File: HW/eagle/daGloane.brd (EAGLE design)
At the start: 182.4 x 160.7 mm, 65 parts, among them IC1 MCP1252-33X50, U1 STM32F10XTXU6, X2 SPARKFUN-CONNECTORS_USB-MICROB

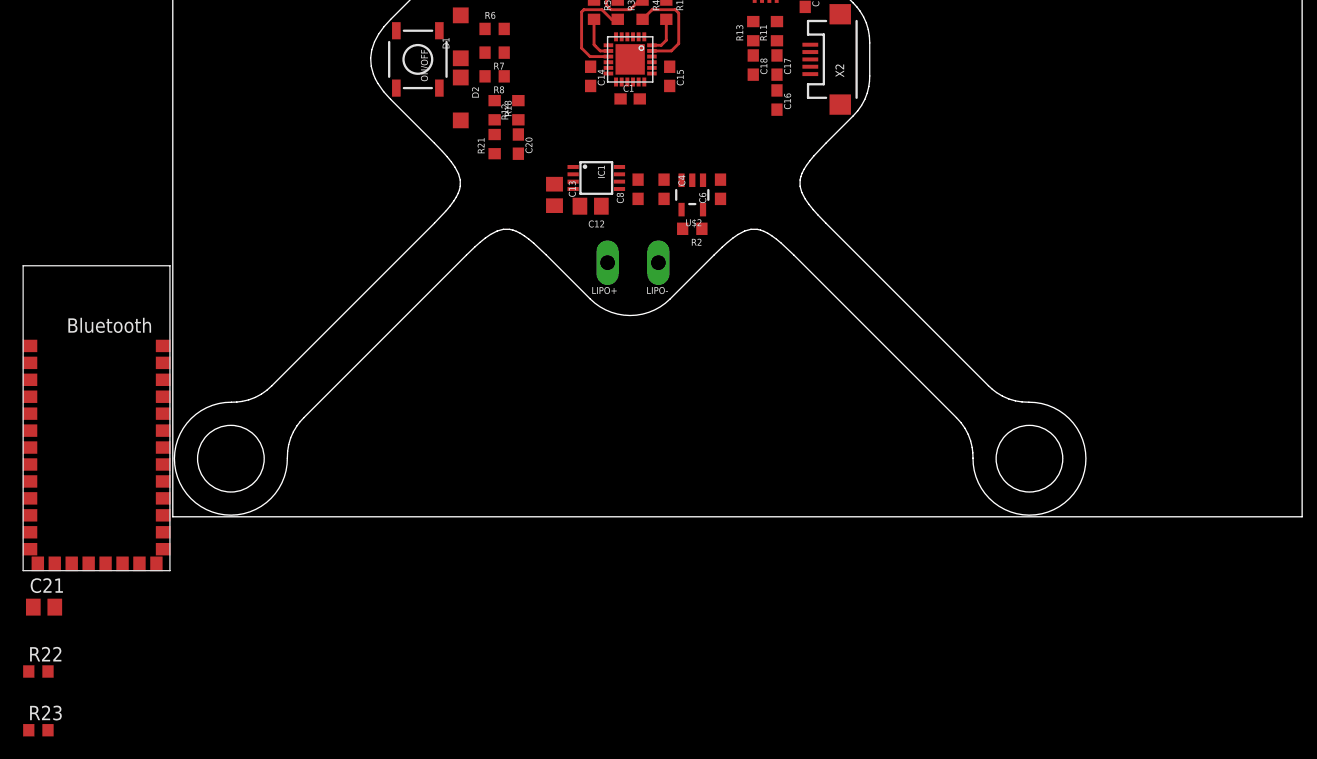
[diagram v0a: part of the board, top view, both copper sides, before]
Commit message: missing connection uart connection to bluetooth module fixed
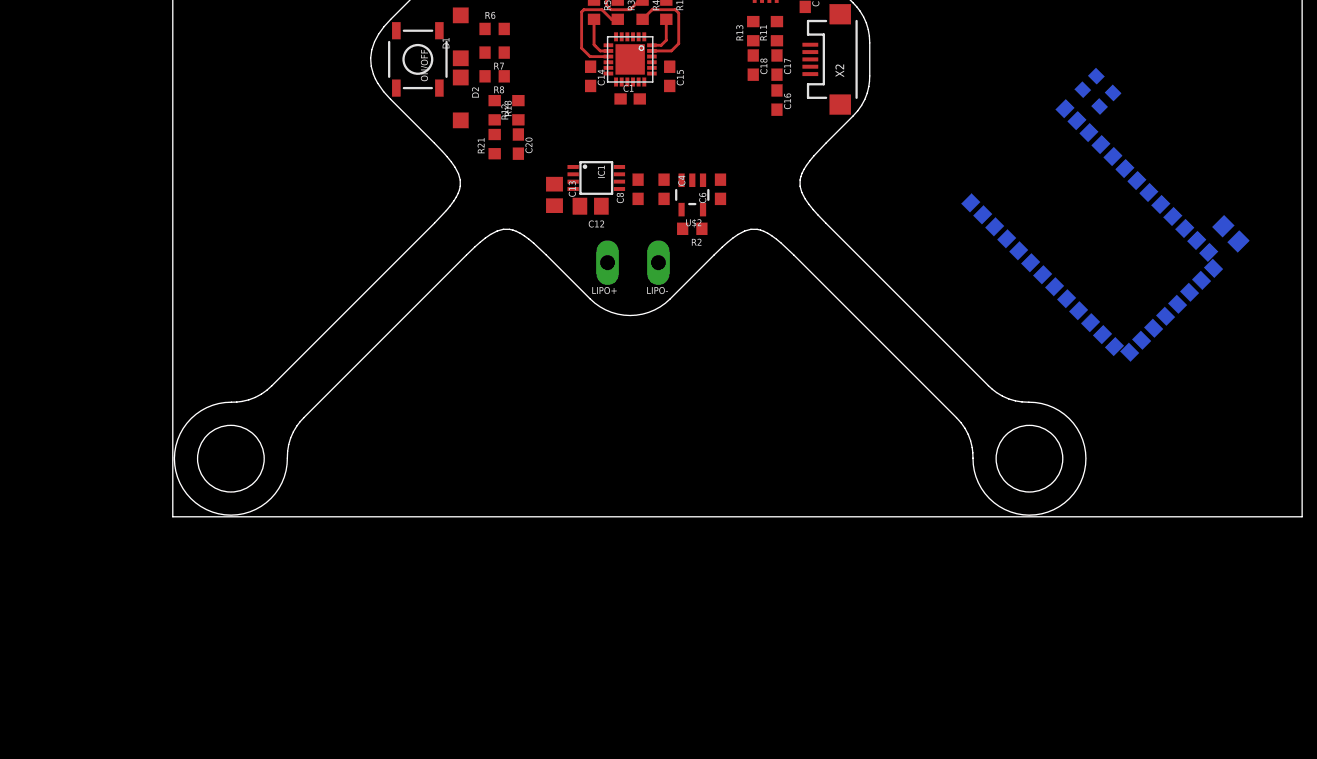
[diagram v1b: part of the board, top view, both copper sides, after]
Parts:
- moved C21 110.2 mm to (93.7, 25.1), flipped to the bottom, turned to 225 degrees
- moved R23 109.8 mm to (82.7, 36.9), flipped to the bottom, turned to 315 degrees
- moved R22 106.7 mm to (81.2, 38.4), flipped to the bottom, turned to 315 degrees
- moved U$5 86.8 mm to (78.0, 29.0), flipped to the bottom, turned to 315 degrees
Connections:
- net USART2_RX: now also R22.1
- net USART2_TX: now also R23.1
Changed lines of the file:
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@@
 <?xml version="1.0" encoding="utf-8"?>
 <!DOCTYPE eagle SYSTEM "eagle.dtd">
-<eagle version="6.2">
+<eagle version="6.1">
 <drawing>
 <settings>
@@
 <board>
 <plain>
-<wire x1="-0.000003125" y1="-4.9999875" x2="0.00000625" y2="-4.999996875" width="0.01" layer="20"/>
 <wire x1="84.99998125" y1="-0.000003125" x2="84.999990625" y2="0.00000625" width="0.01" layer="20"/>
-<wire x1="78.5" y1="84.49998125" x2="78.499990625" y2="84.499990625" width="0.01" layer="20"/>
 <wire x1="0" y1="0" x2="0" y2="80" width="0.01" layer="20"/>
 <wire x1="0" y1="80" x2="100" y2="80" width="0.01" layer="20"/>
@@
 </element>
 <element name="X2" library="daGloane" package="SPARKFUN-CONNECTORS_USB-MICROB" value="SPARKFUN-CONNECTORS_USB-MICROB" x="59.1" y="40.5" rot="R90"/>
-<element name="U$5" library="daGloane" package="BLUETOOTH" value="BLUETOOTH" x="-6.9" y="10.8"/>
-<element name="C21" library="rcl" package="C0805" value="10µF/6.3V" x="-11.4" y="-8"/>
-<element name="R22" library="rcl" package="R0603" value="1k" x="-11.9" y="-13.7"/>
-<element name="R23" library="rcl" package="R0603" value="1k" x="-11.9" y="-18.9"/>
+<element name="U$5" library="daGloane" package="BLUETOOTH" value="BLUETOOTH" x="77.997915625" y="29.01213125" rot="MR315"/>
+<element name="C21" library="rcl" package="C0805" value="10µF/6.3V" x="93.6956875" y="25.05233125" rot="MR225"/>
+<element name="R22" library="rcl" package="R0603" value="1k" x="81.179896875" y="38.41665" rot="MR315"/>
+<element name="R23" library="rcl" package="R0603" value="1k" x="82.664821875" y="36.931725" rot="MR315"/>
 </elements>
 <signals>
@@
 <wire x1="25.95" y1="62" x2="34.7" y2="55.2" width="0" layer="19" extent="1-1"/>
 <wire x1="25.95" y1="66" x2="25.95" y2="62" width="0" layer="19" extent="1-1"/>
-<wire x1="-0.85" y1="-2.87" x2="28.5" y2="32.15" width="0" layer="19" extent="1-1"/>
-<wire x1="-1.45" y1="-4.17" x2="-0.85" y2="-2.87" width="0" layer="19" extent="1-1"/>
-<wire x1="-10.45" y1="-8" x2="-1.45" y2="-4.17" width="0" layer="19" extent="1-1"/>
-<wire x1="-11.95" y1="-4.17" x2="-10.45" y2="-8" width="0" layer="19" extent="1-1"/>
-<wire x1="-12.65" y1="-2.87" x2="-11.95" y2="-4.17" width="0" layer="19" extent="1-1"/>
+<wire x1="83.386071875" y1="15.067984375" x2="28.5" y2="32.15" width="0" layer="19" extent="1-1"/>
+<wire x1="84.729575" y1="14.573009375" x2="83.386071875" y2="15.067984375" width="0" layer="19" extent="1-1"/>
+<wire x1="94.367440625" y1="24.380578125" x2="84.729575" y2="14.573009375" width="0" layer="19" extent="1-1"/>
+<wire x1="92.15419375" y1="21.99763125" x2="94.367440625" y2="24.380578125" width="0" layer="19" extent="1-1"/>
+<wire x1="91.72993125" y1="23.41184375" x2="92.15419375" y2="21.99763125" width="0" layer="19" extent="1-1"/>
 </signal>
 <signal name="LED1">
@@
 <wire x1="35.45" y1="30.325" x2="39.65" y2="37" width="0" layer="19" extent="1-1"/>
 <wire x1="33.8" y1="29.45" x2="35.45" y2="30.325" width="0" layer="19" extent="1-1"/>
-<wire x1="-12.65" y1="0.13" x2="33.8" y2="29.45" width="0" layer="19" extent="1-1"/>
-<wire x1="-12.65" y1="-1.37" x2="-12.65" y2="0.13" width="0" layer="19" extent="1-1"/>
-<wire x1="-12.35" y1="-8" x2="-12.65" y2="-1.37" width="0" layer="19" extent="1-1"/>
+<wire x1="89.608609375" y1="25.533165625" x2="33.8" y2="29.45" width="0" layer="19" extent="1-1"/>
+<wire x1="90.669271875" y1="24.472503125" x2="89.608609375" y2="25.533165625" width="0" layer="19" extent="1-1"/>
+<wire x1="93.0239375" y1="25.72408125" x2="90.669271875" y2="24.472503125" width="0" layer="19" extent="1-1"/>
 </signal>
 <signal name="N$11">
@@
 <signal name="USART2_RX">
 <contactref element="U1" pad="10"/>
+<contactref element="R22" pad="1"/>
+<wire x1="38.5" y1="49.825" x2="81.780940625" y2="39.017690625" width="0" layer="19" extent="1-16"/>
 </signal>
 <signal name="USART2_TX">
 <contactref element="U1" pad="9"/>
+<contactref element="R23" pad="1"/>
+<wire x1="37.725" y1="50.6" x2="83.265865625" y2="37.532765625" width="0" layer="19" extent="1-16"/>
 </signal>
 <signal name="MOT4">
@@
 <contactref element="U$5" pad="P$1"/>
 <contactref element="R22" pad="2"/>
-<wire x1="-12.65" y1="15.13" x2="-11.05" y2="-13.7" width="0" layer="19" extent="1-1"/>
+<wire x1="79.002009375" y1="36.139765625" x2="80.57885625" y2="37.81560625" width="0" layer="19" extent="1-1"/>
 </signal>
 <signal name="N$15">
 <contactref element="U$5" pad="P$2"/>
 <contactref element="R23" pad="2"/>
-<wire x1="-12.65" y1="13.63" x2="-11.05" y2="-18.9" width="0" layer="19" extent="1-1"/>
+<wire x1="80.06266875" y1="35.07910625" x2="82.06378125" y2="36.33068125" width="0" layer="19" extent="1-1"/>
 </signal>
 </signals>

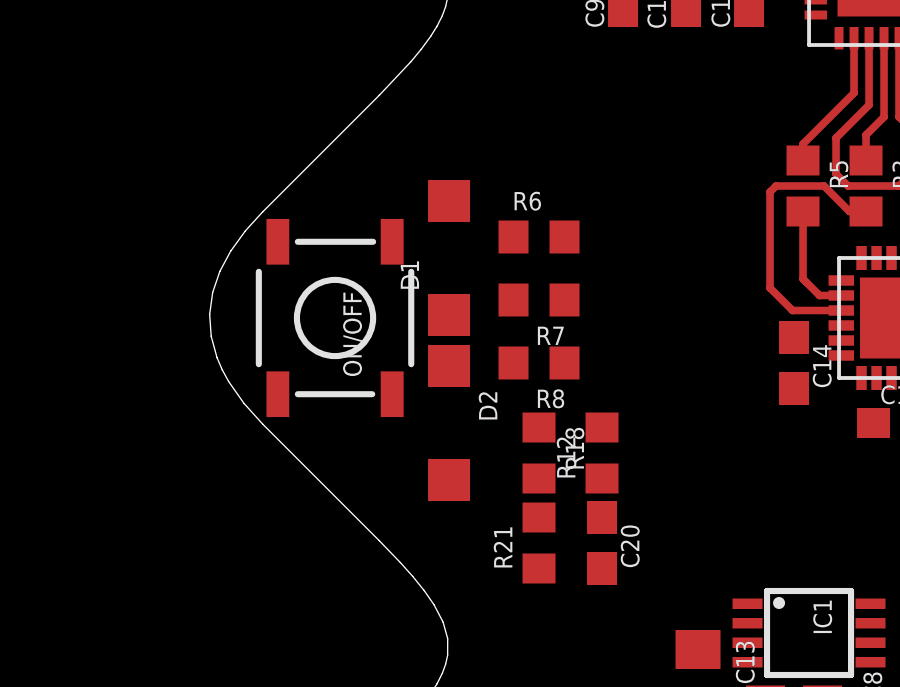
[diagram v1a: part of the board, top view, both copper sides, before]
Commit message: 2 descrete diodes replaced by one part containing to diodes
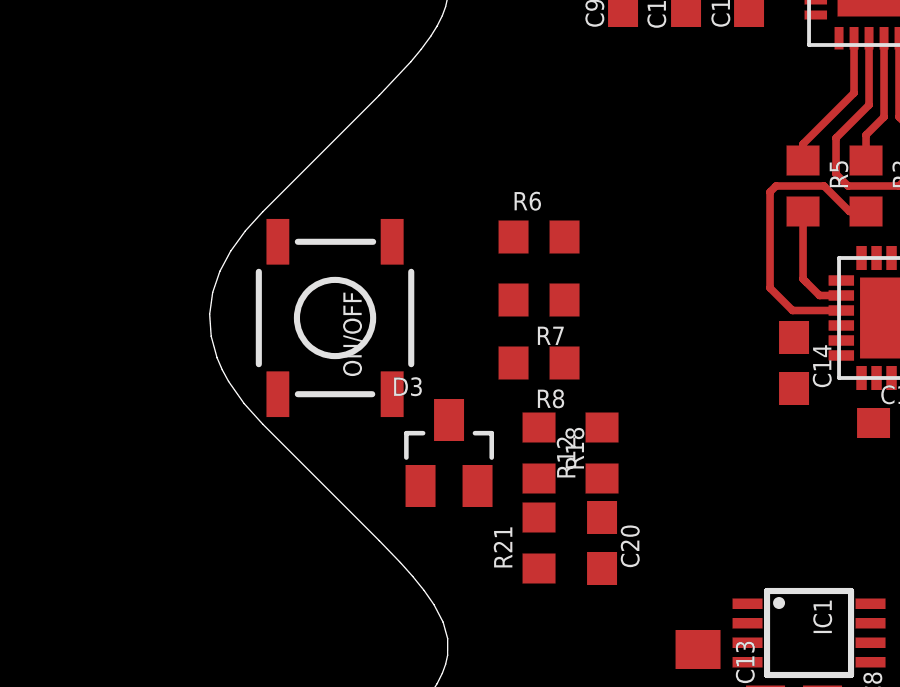
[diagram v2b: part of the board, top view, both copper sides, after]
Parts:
- removed D1, D2: MBR0520LT, diode:SOD123
- added D3: BAT54C, diode:SOT23
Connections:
- new net MOT1: U1.15
- new net MOT2: U1.16
- new net MOT3: U1.31
- net N$23: now also D3.2; no longer D1.A
- net PWR_OFF: now also U1.29
- net PWR_ON: now also D3.3; no longer D1.C, D2.C
- net PWR_ON_µC: now also D3.1, U1.23; no longer D2.A
